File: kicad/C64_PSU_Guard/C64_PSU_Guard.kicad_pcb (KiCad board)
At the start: 2 copper layers, 58 x 44 mm, 50 parts, among them J1 PSU_IN, J2 DRIVE, J3 UFI_LINK, Q1 AO3401A, Q2 2N7002, Q3 AO3401A, Q4 2N7002, U1 TPS25921ADR, U2 TPS25921ADR

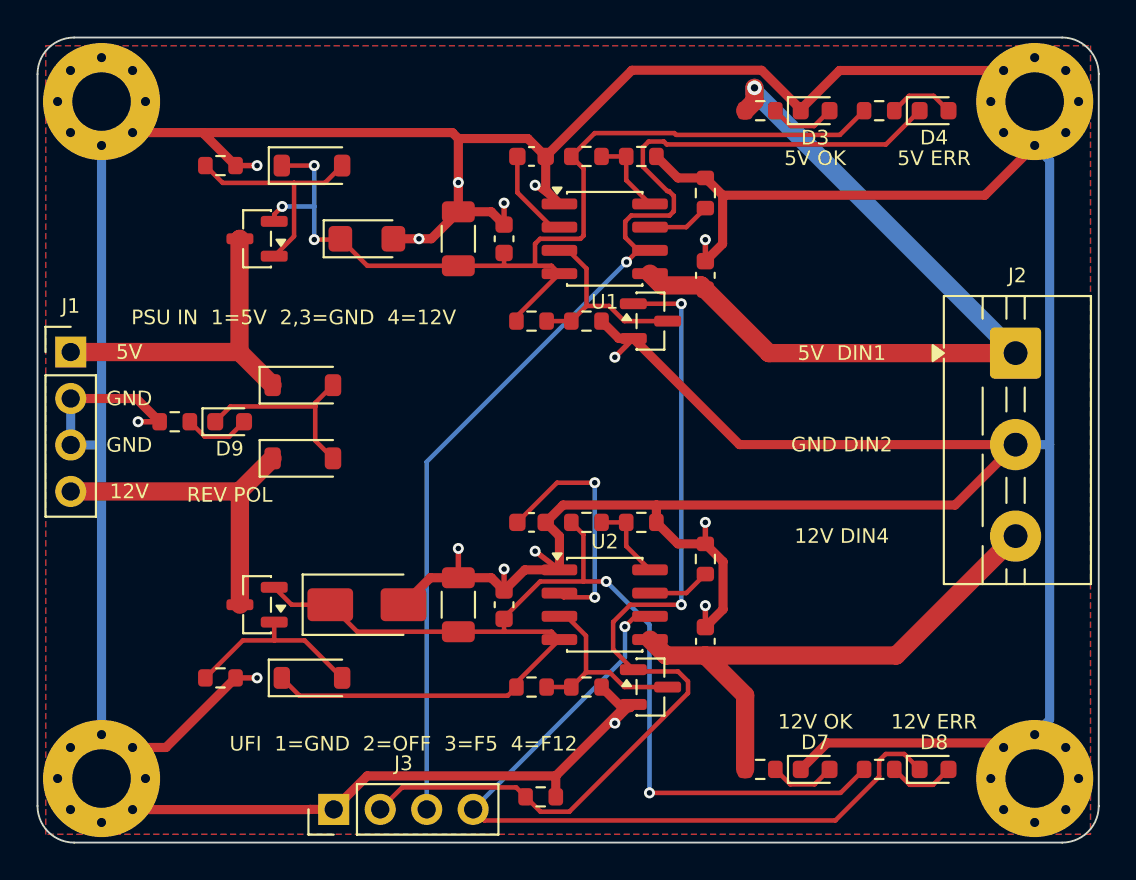
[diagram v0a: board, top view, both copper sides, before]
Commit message: C64 PSU Guard: terminal block J2 turned so the wire openings face the board edge (checked with the Phoenix MKDS 3D model of the same footprint generator; the MaiXu footprint has none), pin-1 marker clear of the edge, LEDs turned anode-to-resistor and gate parts on the gate side so Freerouting closes every net, THT GND single-spoke rule, re-route pass for leftover unconnected nets; fab files regenerated, DRC 0
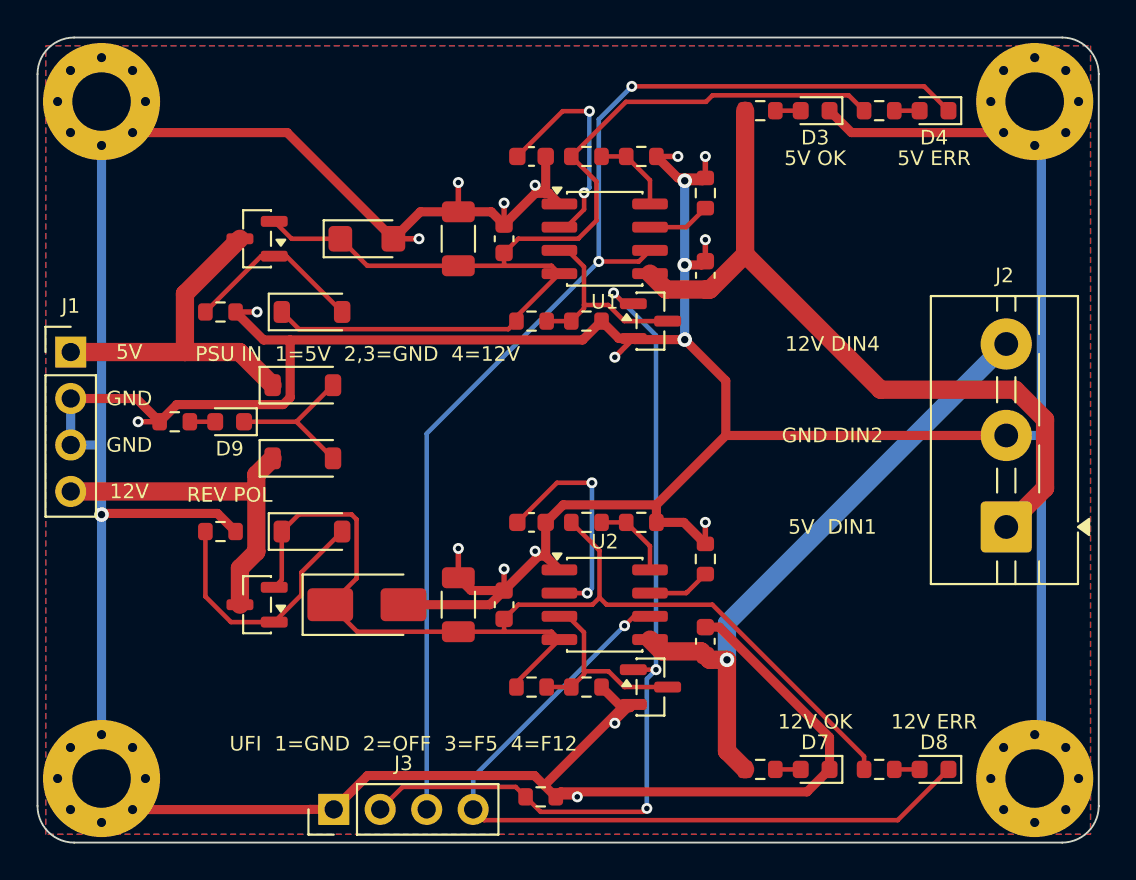
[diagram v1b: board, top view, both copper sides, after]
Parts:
- moved J2 9.51 mm to (52.9, 26.8), turned to 90 degrees
- moved D1 8.00 mm to (15.0, 15.0)
- moved D5 8.00 mm to (15.0, 27.0)
- moved R1 8.00 mm to (10.0, 15.0)
- moved R9 8.00 mm to (10.0, 27.0)
- turned D3 to 180 degrees
- turned D4 to 180 degrees
- turned D7 to 180 degrees
- turned D8 to 180 degrees
- turned D9 to 180 degrees
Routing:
- net GND: track 390.5 -> 380.3 mm, vias 15 -> 20
- net /V12_P: track 69.2 -> 59.9 mm, vias 2 -> 0
- net /V5_P: track 52.8 -> 62.0 mm, vias 3 -> 0
- net /SS5: track 5.06 -> 12.2 mm, vias 0 -> 2
- net +12V_OUT: track 30.2 -> 34.6 mm, vias 0 -> 1
- net /G12: track 10.2 -> 14.4 mm
- net FLT5: track 61.1 -> 65.1 mm, vias 1 -> 2
- net OFF: track 50.7 -> 47.6 mm, vias 2 -> 3
- net /G5: track 12.7 -> 10.0 mm
- net +5V_OUT: track 43.7 -> 41.1 mm, vias 1 -> 0
- net /LR12: track 3.66 -> 1.39 mm
- net /LG5: track 3.66 -> 1.39 mm
- net /LG12: track 3.64 -> 1.39 mm
- net /LR5: track 3.64 -> 1.39 mm
- net /REVA: track 3.64 -> 1.39 mm
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
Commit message: C64 PSU Guard: external LED header J4 (2x5, one pair per LED with own series resistor R19-R23, parallel to the on-board LEDs), J3 ERR5/ERR12 now open-drain outputs through 2N7002 inverters Q5/Q6 (the eFuse FLT nodes sit at rail voltage via the red LED chains, up to 12 V, so they must not reach a 3.3 V input directly; high = fault or guard unpowered), README: mapping to UFI Headless J9 (PB6/PB7 with their 2.2k pull-ups, PE0 as OFF); headers 0.5/1 mm off the edge, island vias for pour fragments, GND single-spoke rule for all GND pads, 40 router passes; ERC/DRC 0, fab files regenerated
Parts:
- added J4: EXT_LED, Connector_PinHeader_2.54mm:PinHeader_2x05_P2.54mm_Vertical, F.Cu at (11.9, 4.87)
- added Q5: 2N7002, Package_TO_SOT_SMD:SOT-23, F.Cu at (31.0, 41.5)
- added Q6: 2N7002, Package_TO_SOT_SMD:SOT-23, F.Cu at (35.5, 41.5)
- added R19: 1k, Resistor_SMD:R_0603_1608Metric, F.Cu at (11.0, 7.50)
- added R20: 1k, Resistor_SMD:R_0603_1608Metric, F.Cu at (14.1, 7.50)
- added R21: 3.3k, Resistor_SMD:R_0603_1608Metric, F.Cu at (17.2, 7.50)
- added R22: 3.3k, Resistor_SMD:R_0603_1608Metric, F.Cu at (20.3, 7.50)
- added R23: 2.2k, Resistor_SMD:R_0603_1608Metric, F.Cu at (23.4, 7.50)
- moved J3 1.00 mm to (16.2, 41.2)
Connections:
- J3 pad 3: FLT5 -> /ERR5
- J3 pad 4: FLT12 -> /ERR12
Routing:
- net FLT5: track 65.1 -> 108.1 mm, vias 2 -> 4
- net +12V_OUT: track 34.6 -> 75.9 mm, vias 1 -> 2
- net +5V_OUT: track 41.1 -> 81.7 mm
- net /V12_P: track 59.9 -> 99.0 mm, vias 0 -> 4
- net GND: track 380.3 -> 351.6 mm, vias 20 -> 12
- net FLT12: track 42.4 -> 67.8 mm, vias 1 -> 2
- net /REV: track 8.52 -> 30.5 mm, vias 0 -> 1
- net /ERR12: track 0.00 -> 12.9 mm, vias 0 -> 1
- net /ERR5: track 0.00 -> 12.1 mm
- net /G5: track 10.0 -> 17.2 mm, vias 0 -> 2
- net OFF: track 47.6 -> 54.0 mm, vias 3 -> 2
- net /SS5: track 12.2 -> 6.87 mm
- net /EN12: track 11.3 -> 15.7 mm, vias 0 -> 3
- net /OV12: track 4.48 -> 8.55 mm, vias 0 -> 2
- net /XREV: track 0.00 -> 3.52 mm
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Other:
- board text added: "EXT LED +odd -even"
- board text added: "UFI 1=GND 2=OFF 3=ERR5 4=ERR12"
- board text removed: "UFI 1=GND 2=OFF 3=F5 4=F12"

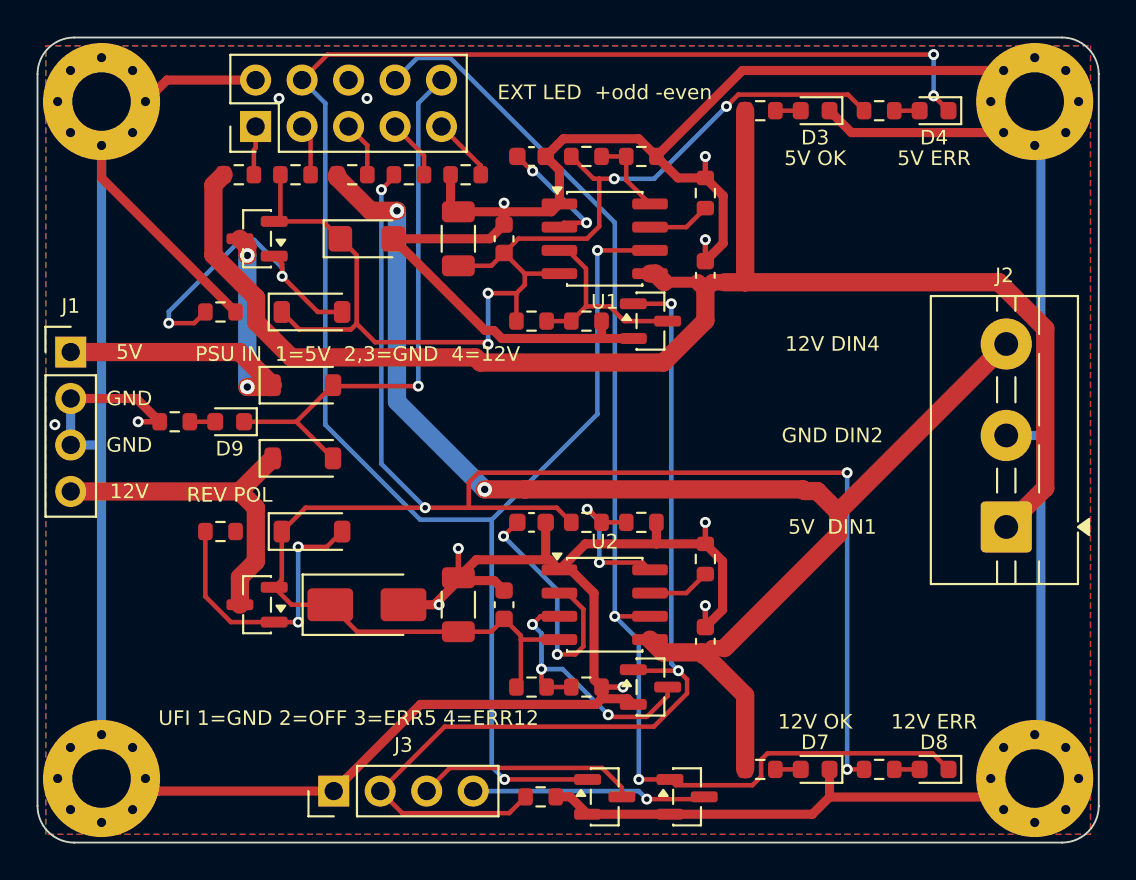
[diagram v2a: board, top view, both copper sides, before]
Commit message: C64 PSU Guard: one external fault LED instead of the 2x5 LED header - J4 1x2 (1 = +, 2 = -), 1k from the protected 5 V input, cathode through a 1N4148W diode OR (D12/D13) into both eFuse FLT outputs: on while either channel is switched off; README, fab files regenerated, ERC/DRC 0
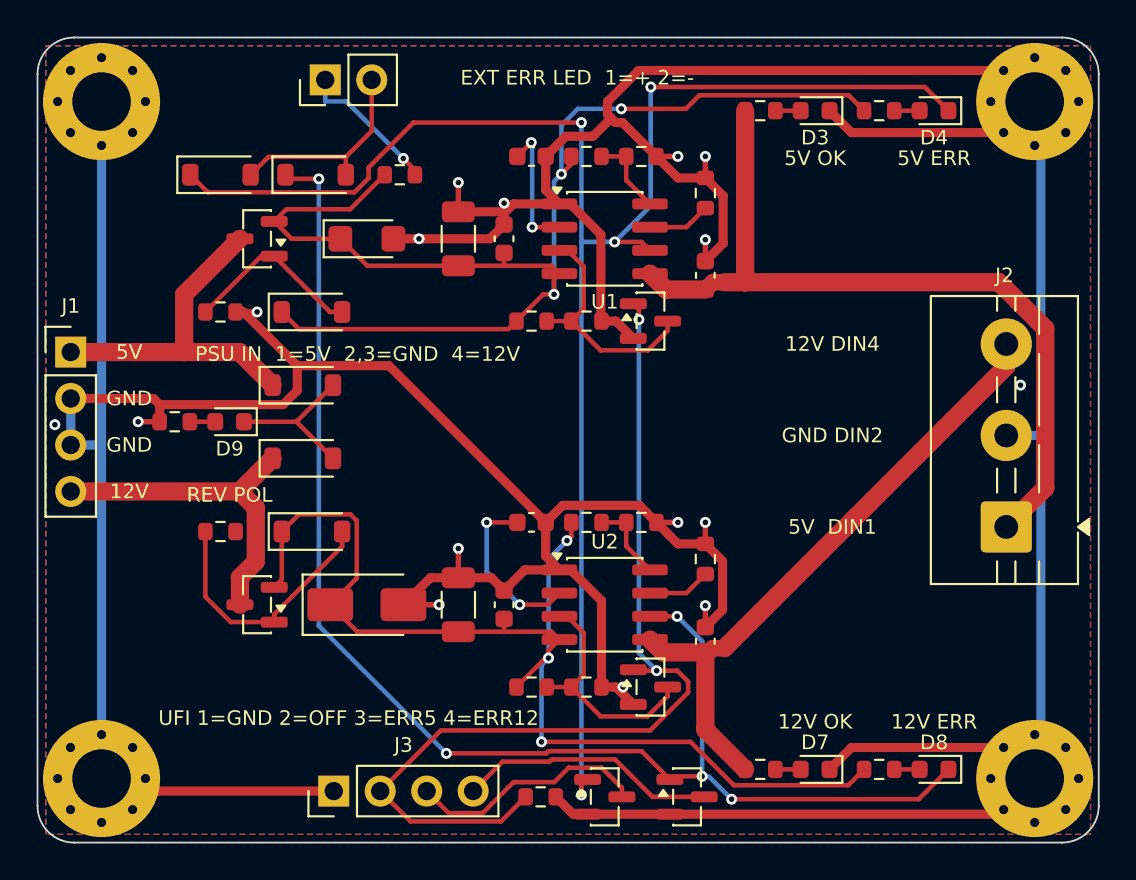
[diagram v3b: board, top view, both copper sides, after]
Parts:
- removed R20: 1k, Resistor_SMD:R_0603_1608Metric
- removed R21, R22: 3.3k, Resistor_SMD:R_0603_1608Metric
- removed R23: 2.2k, Resistor_SMD:R_0603_1608Metric
- added D12: 1N4148W, Diode_SMD:D_SOD-123, F.Cu at (10.0, 7.50)
- added D13: 1N4148W, Diode_SMD:D_SOD-123, F.Cu at (15.2, 7.50)
- J4: value EXT_LED -> EXT_ERR; footprint Connector_PinHeader_2.54mm:PinHeader_2x05_P2.54mm_Vertical -> Connector_PinHeader_2.54mm:PinHeader_1x02_P2.54mm_Vertical
- moved R19 8.80 mm to (19.8, 7.50)
- moved J4 4.58 mm to (15.7, 2.31)
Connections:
- net /X5G renamed /XA
- J4 pad 2: GND -> /XK
- R19 pad 1: +5V_OUT -> /V5_P
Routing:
- net +12V_OUT: track 75.9 -> 34.7 mm, vias 2 -> 0
- net +5V_OUT: track 81.7 -> 44.3 mm
- net /V12_P: track 99.0 -> 62.4 mm, vias 4 -> 3
- net /REV: track 30.5 -> 8.52 mm, vias 1 -> 0
- net FLT5: track 108.1 -> 91.5 mm
- net /XK: track 0.00 -> 11.4 mm
- net FLT12: track 67.8 -> 76.4 mm, vias 2 -> 5
- net /G5: track 17.2 -> 10.0 mm, vias 2 -> 0
- net /V5_P: track 64.4 -> 70.0 mm, vias 4 -> 3
- net /XA: track 2.67 -> 7.89 mm, vias 0 -> 1
- net /SS12: track 14.1 -> 9.36 mm
- net /OV12: track 8.55 -> 4.48 mm, vias 2 -> 0
- net /XREV: track 3.52 -> 0.00 mm
- net /X12R: track 3.29 -> 0.00 mm
- net GND: track 351.6 -> 354.8 mm, vias 12 -> 16
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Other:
- board text added: "EXT ERR LED 1=+ 2=-"
- board text removed: "EXT LED +odd -even"

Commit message: C64 PSU Guard v0.2 stage G2 (layout), review finding 3 and the new parts: the load nets are net class Load (1.0 mm, vias 0.8/0.4) in .kicad_pro: +5V_IN, +12V_IN, /V5_P, /V12_P, +5V_OUT, +12V_OUT. Root cause of the 0.25 mm intermediate nodes in v0.1: build_pcb.py assigned the pattern "V5_P"/"V12_P", but the local nets are named "/V5_P"/"/V12_P", so they fell into the default class. The main load paths are now pre-routed in build_pcb.py as locked 1.0 mm F.Cu tracks (Freerouting keeps them): J1 -> Q drain, Q source -> TVS -> 10 uF -> 100 nF -> U IN, U OUT -> 1 uF -> J2; only +5V_OUT changes to B.Cu behind C4, through a locked via pair. finish_pcb.py restores 1.0 mm on Freerouting-necked Load segments where the clearance allows (2 widened this run, 0 left narrow). Placement: J1 and J3 JST XH B4B-XH-A footprints (J1 rot 270, pin 1 +5V at the top; J3 pin 1 GND left), REV-POL group R17/D9/D10/D11 moved right of the wider J1 housing, R20/R21 next to the channel dividers. Silkscreen: back "C64 PSU Guard v0.2 2026-10-26" plus the J3 = UFI J20 pin legend, front "UFI J20", J1 pin labels moved clear of the XH outline. D6 field "Description" moved to "Note" (parity). make_pcb.sh: 4 re-route rounds for leftover connections. New routing_rules.json (min_width 1.0 on all six load nets, min_vias 2 on +5V_OUT, 16 paths covering every hop incl. the intermediate nodes). Gates: ERC --severity-all 0/0; DRC --severity-all --schematic-parity 0 violations / 0 unconnected / 0 parity; check_routing.py exit 0, 0 FEHLER, 0 HALS, every path OK at >= 1.0 mm: 5 V J1->Q1 12.2 mm ~6 mOhm, Q1->U1 IN 19.0 mm ~9 mOhm (v0.1 16.8 mm ~34 mOhm), U1 OUT->C4 3.4 mm, C4->J2 23.4 mm ~11 mOhm; 12 V J1->Q3 12.2 mm, Q3->U2 IN 19.0 mm ~9 mOhm (v0.1 26.4 mm ~52 mOhm), U2 OUT->C8 3.4 mm, C8->J2 28.3 mm ~14 mOhm. Branch connections of the load nets (dividers, LED / pull-up resistors, <= 3 mA) are Freerouting tracks at 1.0 mm, two of them change layer through single vias (+5V_OUT -> R7: one via, +12V_OUT -> R15: a B.Cu 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
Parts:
- added R20: 100k, Resistor_SMD:R_0603_1608Metric, F.Cu at (23.5, 6.50)
- added R21: 100k, Resistor_SMD:R_0603_1608Metric, F.Cu at (23.5, 26.5)
- D6: value SMAJ15CA -> SMAJ13A
- J1, J3: footprint Connector_PinHeader_2.54mm:PinHeader_1x04_P2.54mm_Vertical -> Connector_JST:JST_XH_B4B-XH-A_1x04_P2.50mm_Vertical
- moved D10 2.50 mm to (17.0, 19.0)
- moved D11 2.50 mm to (17.0, 23.0)
- moved D9 2.50 mm to (13.0, 21.0)
- moved R17 2.50 mm to (10.0, 21.0)
- moved J1 2.13 mm to (3.94, 17.2), turned to -90 degrees
- moved J3 1.88 mm to (15.2, 39.6), turned to 0 degrees
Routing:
- net GND: track 354.8 -> 372.5 mm
- net +5V_IN: track 19.2 -> 35.9 mm
- net /OV5: track 4.48 -> 16.2 mm, vias 0 -> 2
- net +12V_OUT: track 34.7 -> 45.9 mm, vias 0 -> 2
- net FLT12: track 76.4 -> 66.4 mm, vias 5 -> 6
- net /V12_P: track 62.4 -> 71.4 mm, vias 3 -> 0
- net /V5_P: track 70.0 -> 62.6 mm, vias 3 -> 0
- net +5V_OUT: track 44.3 -> 39.3 mm, vias 0 -> 3
- net +12V_IN: track 18.7 -> 21.8 mm
- net /G5: track 10.0 -> 12.3 mm
- net /G12: track 14.4 -> 16.5 mm, vias 0 -> 2
- net /EN12: track 13.2 -> 11.2 mm
- net /EN5: track 13.2 -> 11.2 mm
- net /XA: track 7.89 -> 9.80 mm
- net FLT5: track 91.5 -> 93.1 mm
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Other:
- board text added: "C64 PSU Guard v0.2 2026-10-26"
- board text added: "J3 = UFI J20: 1 GND 2 OFF 3 ERR5 4 ERR12"
- board text added: "PSU IN"
- board text added: "UFI J20"
- board text removed: "C64 PSU Guard v0.1"
- board text removed: "PSU IN 1=5V 2,3=GND 4=12V"
- board text removed: "UFI 1=GND 2=OFF 3=ERR5 4=ERR12"
